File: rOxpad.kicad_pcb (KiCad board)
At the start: 2 copper layers, 77.8 x 63.5 mm, 22 parts, among them SW1 SW_Push, U1 ATmega32U4-A, Y1 16MHz

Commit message: might've forgot to save whoops
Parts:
- moved F1 83.7 mm to (107.2, 52.4), turned to 0 degrees
- moved C5 63.7 mm to (78.9, 106.6), turned to -90 degrees
- moved R4 61.6 mm to (93.5, 81.8), turned to 45 degrees
- moved C6 61.4 mm to (84.9, 100.0), turned to 45 degrees
- moved C2 60.5 mm to (82.6, 106.6), turned to -90 degrees
- moved U1 54.7 mm to (96.0, 92.1), turned to 45 degrees
- moved C1 53.1 mm to (86.4, 106.6), turned to -90 degrees
- moved MX1 50.1 mm to (76.8, 69.1)
- moved MX2 50.1 mm to (96.0, 69.1)
- moved MX3 50.1 mm to (115.1, 69.1)
- moved D1 49.0 mm to (85.1, 69.1)
- moved D2 49.0 mm to (104.1, 69.1)
- moved D3 49.0 mm to (123.2, 69.1)
- moved SW1 48.0 mm to (118.3, 92.9), turned to 180 degrees
- moved R1 46.2 mm to (106.4, 56.4), turned to 0 degrees
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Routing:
- net +5V: track 0.48 -> 79.0 mm, vias 0 -> 2
- net GND: track 0.61 -> 76.6 mm
- net ROW-0: track 0.00 -> 72.4 mm
- net Net-(R1-Pad2): track 0.00 -> 64.4 mm, vias 0 -> 2
- net Net-(R2-Pad2): track 0.00 -> 57.2 mm, vias 0 -> 2
- net COL-0: track 0.00 -> 49.1 mm
- net Net-(R3-Pad2): track 0.00 -> 37.1 mm
- net COL-2: track 0.00 -> 36.0 mm, vias 0 -> 2
- net COL-1: track 0.00 -> 32.5 mm, vias 0 -> 1
- net Net-(C6-Pad1): track 0.00 -> 15.6 mm, vias 0 -> 2
- net Net-(C3-Pad2): track 0.22 -> 12.9 mm
- net Net-(F1-Pad1): track 0.00 -> 9.07 mm
- net D+: track 2.60 -> 10.5 mm
- net Net-(R4-Pad2): track 0.00 -> 7.08 mm
- net Net-(D1-Pad2): track 0.00 -> 6.94 mm
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
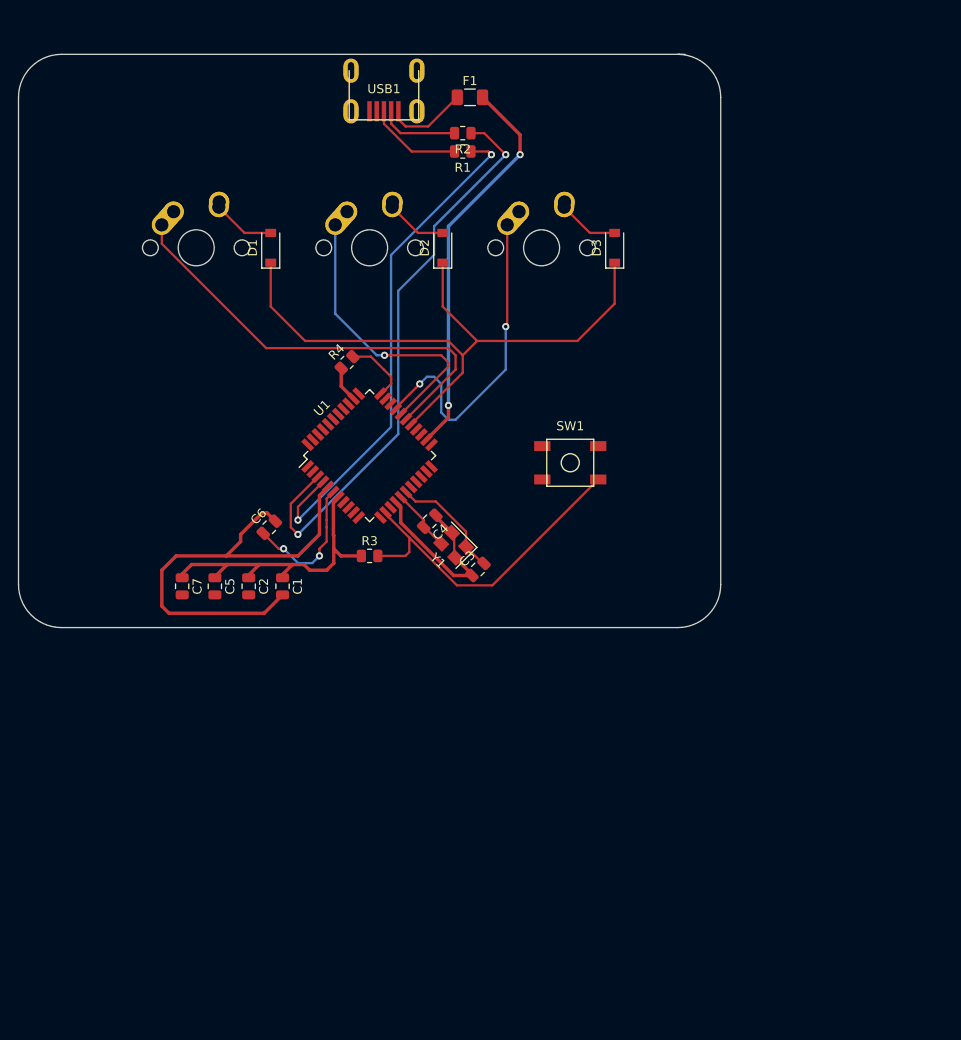
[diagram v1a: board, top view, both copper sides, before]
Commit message: started redesigning the schematic
didn't like the result lol
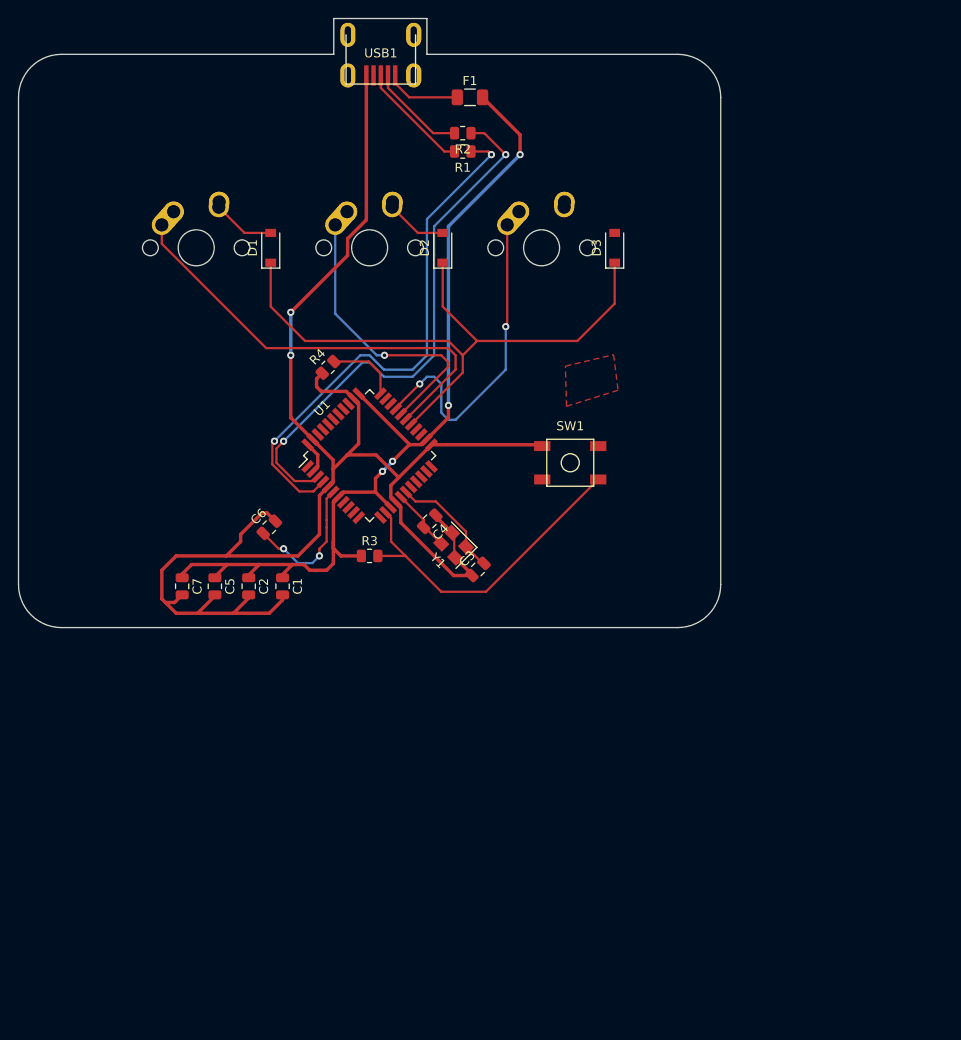
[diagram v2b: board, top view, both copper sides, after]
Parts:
- moved USB1 3.98 mm to (97.3, 45.5)
- moved R4 2.17 mm to (91.4, 82.3)
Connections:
- net Net-(C3-Pad2) renamed XTAL1
- net Net-(C4-Pad2) renamed XTAL2
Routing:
- net GND: track 76.6 -> 174.6 mm, vias 0 -> 2
- net +5V: track 79.0 -> 107.0 mm, vias 2 -> 4
- net Net-(D3-Pad2): track 6.78 -> 0.00 mm
- net Net-(R1-Pad2): track 64.4 -> 60.6 mm
- net Net-(R2-Pad2): track 57.2 -> 59.9 mm
- net D-: track 8.83 -> 10.8 mm
- net D+: track 10.5 -> 12.5 mm
- net Net-(R4-Pad2): track 7.08 -> 7.96 mm
- net Net-(F1-Pad1): track 9.07 -> 8.39 mm
- added copper zone on F.Cu, net GND
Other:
- board size 77.8 x 63.5 mm -> 77.8 x 67.5 mm

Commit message: I think it's finished wohoo
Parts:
- added R5: 5.1k, Resistor_SMD:R_0805_2012Metric_Pad1.20x1.40mm_HandSolder, F.Cu at (109.5, 72.2)
- added R6: 5.1k, Resistor_SMD:R_0805_2012Metric_Pad1.20x1.40mm_HandSolder, F.Cu at (100.0, 72.2)
- added U2: PRTR5V0U2X, random-keyboard-parts:SOT143B, F.Cu at (100.0, 76.2)
- C1: value 0.1uF -> 1uF; footprint Capacitor_SMD:C_0805_2012Metric -> Capacitor_SMD:C_0805_2012Metric_Pad1.18x1.45mm_HandSolder
- C2: value 0.1uF -> 22Pf; footprint Capacitor_SMD:C_0805_2012Metric -> Capacitor_SMD:C_0805_2012Metric_Pad1.18x1.45mm_HandSolder
- C3, C5: footprint Capacitor_SMD:C_0805_2012Metric -> Capacitor_SMD:C_0805_2012Metric_Pad1.18x1.45mm_HandSolder
- C4: value 22Pf -> 0.1uF; footprint Capacitor_SMD:C_0805_2012Metric -> Capacitor_SMD:C_0805_2012Metric_Pad1.18x1.45mm_HandSolder
- C6: value 1uF -> 0.1uF; footprint Capacitor_SMD:C_0805_2012Metric -> Capacitor_SMD:C_0805_2012Metric_Pad1.18x1.45mm_HandSolder
- C7: value 0.1uF -> 10uF; footprint Capacitor_SMD:C_0805_2012Metric -> Capacitor_SMD:C_0805_2012Metric_Pad1.18x1.45mm_HandSolder
- F1: value 500mA -> Polyfuse_Small; footprint Fuse:Fuse_1206_3216Metric -> Fuse:Fuse_1206_3216Metric_Pad1.42x1.75mm_HandSolder
- MX1, MX2, MX3: footprint MX_Alps_Hybrid:MX-1U-NoLED -> MX_Only:MXOnly-1U-Hotswap
- R1, R2, R3, R4: footprint Resistor_SMD:R_0805_2012Metric -> Resistor_SMD:R_0805_2012Metric_Pad1.20x1.40mm_HandSolder
- U1: value ATmega32U4-A -> ATmega16U2-A; footprint Package_QFP:TQFP-44_10x10mm_P0.8mm -> Package_QFP:TQFP-32_7x7mm_P0.8mm
- USB1: value Molex-0548190589 -> HRO-TYPE-C-31-M-12; footprint random-keyboard-parts:Molex-0548190589 -> Type-C:HRO-TYPE-C-31-M-12-HandSoldering
- moved C7 42.2 mm to (117.4, 108.3), turned to -135 degrees
- moved R4 38.1 mm to (97.6, 119.9), turned to 135 degrees
- moved C5 34.1 mm to (112.9, 103.8), turned to -135 degrees
- moved C1 33.2 mm to (119.1, 112.4), turned to -135 degrees
- moved C6 30.8 mm to (115.2, 106.0), turned to -135 degrees
- moved R3 27.8 mm to (119.1, 118.8), turned to 180 degrees
- moved U1 25.3 mm to (107.2, 114.8), turned to -45 degrees
- moved SW1 22.8 mm to (128.6, 113.2), turned to 0 degrees
- moved MX1 22.8 mm to (88.1, 88.9)
- moved MX2 22.7 mm to (107.2, 88.9)
- moved MX3 22.7 mm to (126.2, 88.9)
- moved C2 22.0 mm to (104.4, 103.3), turned to 135 degrees
- moved D1 21.6 mm to (95.2, 88.1)
- moved D2 21.6 mm to (114.3, 88.1)
- moved D3 21.6 mm to (133.3, 88.1)
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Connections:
- C1 pad 1: +5V -> Net-(C1-Pad1)
- C2 pad 1: +5V -> GND
- C2 pad 2: GND -> XTAL1
- C3 pad 2: XTAL1 -> XTAL2
- C4 pad 1: GND -> +5V
- C4 pad 2: XTAL2 -> GND
- C6 pad 1: Net-(C6-Pad1) -> +5V
- D1 pad 1: ROW-0 -> GND
- D2 pad 1: ROW-0 -> GND
- D3 pad 1: ROW-0 -> GND
- F1 pad 1: Net-(F1-Pad1) -> VCC
- MX1 pad 1: COL-0 -> KEY-0
- MX2 pad 1: COL-1 -> KEY-1
- MX3 pad 1: COL-2 -> KEY-2
- R4 pad 1: GND -> Net-(R4-Pad1)
- R4 pad 2: Net-(R4-Pad2) -> GND
- U1 pad 1: unconnected-(U1-Pad1) -> XTAL1
- U1 pad 13: Net-(R3-Pad2) -> Net-(R4-Pad1)
- U1 pad 14: +5V -> unconnected-(U1-Pad14)
- U1 pad 15: GND -> unconnected-(U1-Pad15)
- U1 pad 16: XTAL2 -> unconnected-(U1-Pad16)
- U1 pad 17: XTAL1 -> unconnected-(U1-Pad17)
- U1 pad 19: unconnected-(U1-Pad19) -> KEY-0
- U1 pad 2: +5V -> XTAL2
- U1 pad 20: unconnected-(U1-Pad20) -> KEY-1
- U1 pad 21: unconnected-(U1-Pad21) -> KEY-2
- U1 pad 23: GND -> unconnected-(U1-Pad23)
- U1 pad 24: +5V -> Net-(R3-Pad2)
- U1 pad 27: ROW-0 -> Net-(C1-Pad1)
- U1 pad 28: COL-0 -> GND
- U1 pad 29: COL-1 -> Net-(R2-Pad2)
- U1 pad 3: Net-(R1-Pad2) -> GND
- U1 pad 30: COL-2 -> Net-(R1-Pad2)
- U1 pad 31: unconnected-(U1-Pad31) -> +5V
- U1 pad 32: unconnected-(U1-Pad32) -> +5V
- U1 pad 4: Net-(R2-Pad2) -> +5V
- U1 pad 5: GND -> unconnected-(U1-Pad5)
- U1 pad 6: Net-(C6-Pad1) -> unconnected-(U1-Pad6)
- U1 pad 7: +5V -> unconnected-(U1-Pad7)
- USB1 pad 2: unconnected-(USB1-Pad2) -> VCC
- USB1 pad 3: D+ -> unconnected-(USB1-Pad3)
- USB1 pad 4: D- -> Net-(R5-Pad1)
- USB1 pad 5: Net-(F1-Pad1) -> D-
- USB1 pad 6: unconnected-(USB1-Pad6) -> D+
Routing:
- net ROW-0: track 72.4 -> 0.00 mm
- net KEY-2: track 0.00 -> 66.1 mm, vias 0 -> 1
- net KEY-0: track 0.00 -> 63.3 mm, vias 0 -> 1
- net COL-0: track 49.1 -> 0.00 mm
- net KEY-1: track 0.00 -> 48.0 mm, vias 0 -> 1
- net VCC: track 0.00 -> 42.7 mm, vias 0 -> 2
- net COL-2: track 36.0 -> 0.00 mm, vias 2 -> 0
- net COL-1: track 32.5 -> 0.00 mm, vias 1 -> 0
- net +5V: track 107.0 -> 80.6 mm, vias 4 -> 2
- net Net-(R3-Pad2): track 37.1 -> 19.8 mm
- net Net-(C6-Pad1): track 15.6 -> 0.00 mm, vias 2 -> 0
- net Net-(R2-Pad2): track 59.9 -> 75.5 mm
- net Net-(C1-Pad1): track 0.00 -> 14.0 mm
- net Net-(R1-Pad2): track 60.6 -> 72.5 mm
- net Net-(F1-Pad1): track 8.39 -> 0.00 mm
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- removed copper zone on F.Cu, net GND
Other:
- board size 77.8 x 67.5 mm -> 68.3 x 65.1 mm

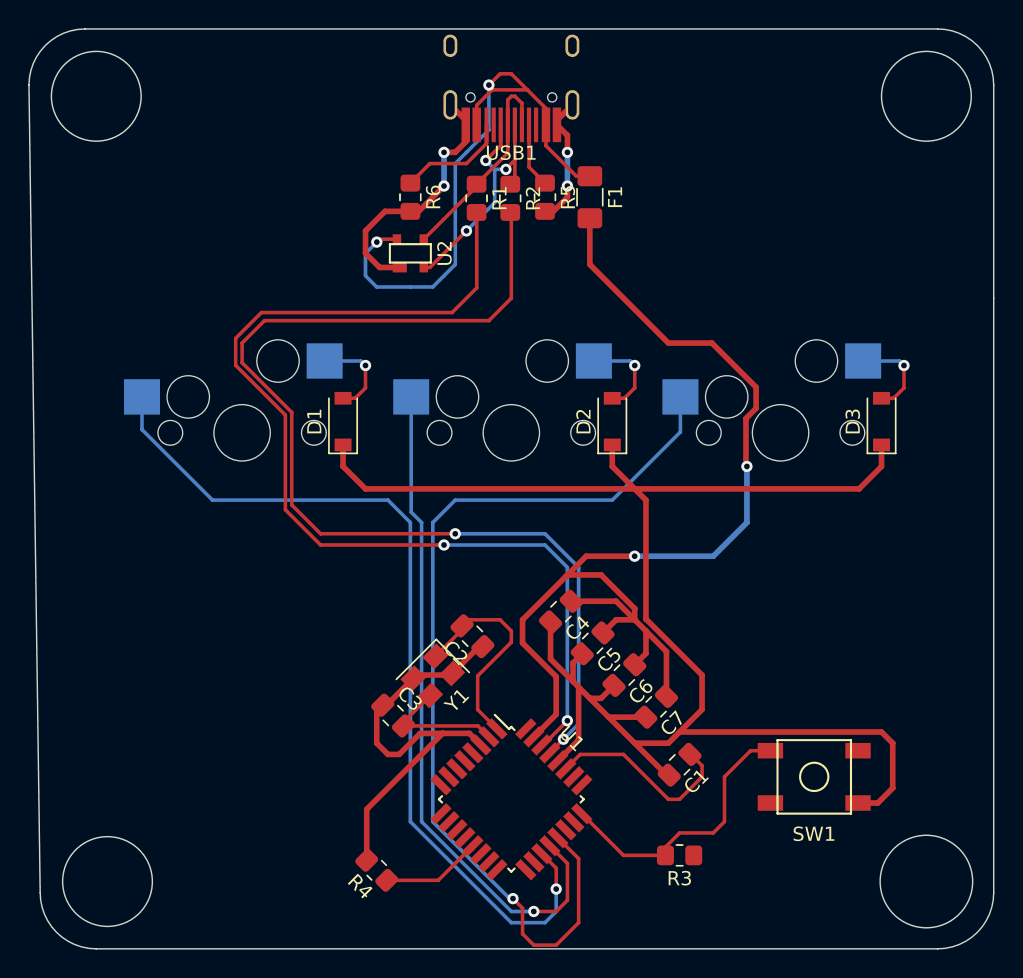
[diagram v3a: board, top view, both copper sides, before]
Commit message: create gitignore and change hole size
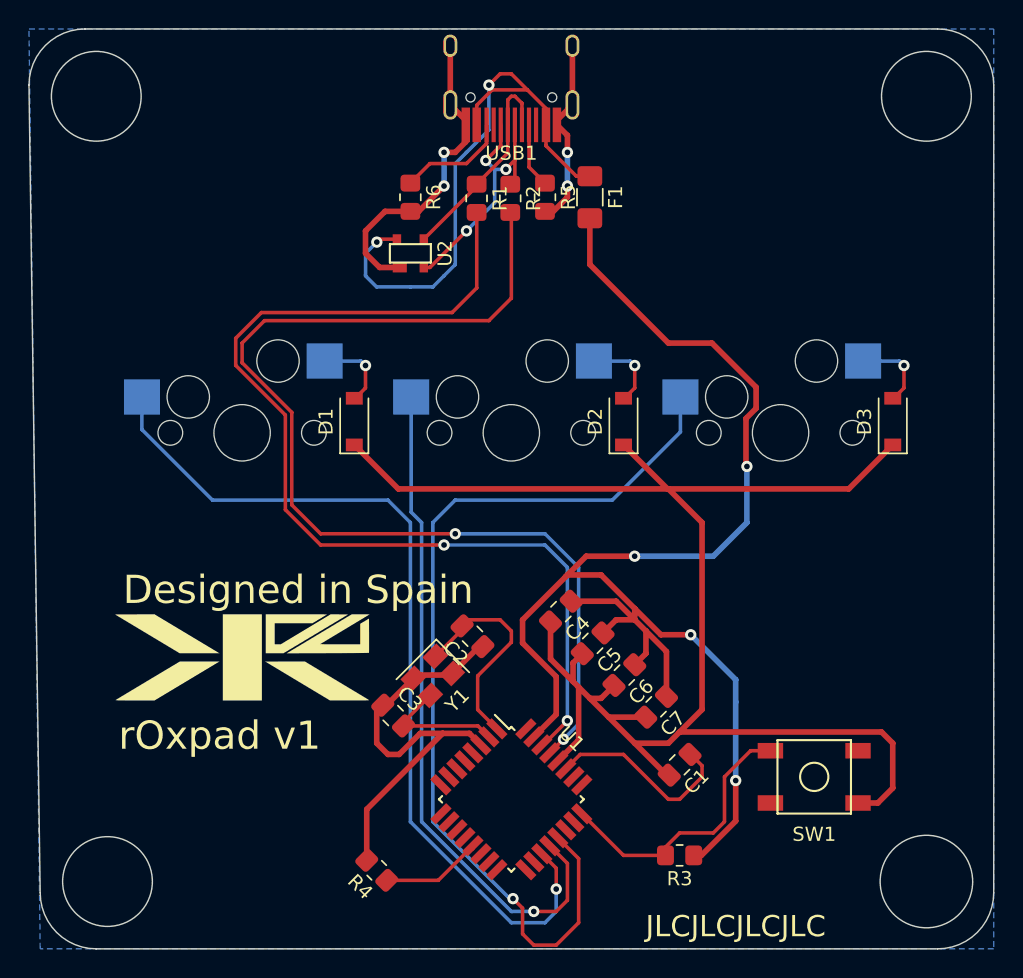
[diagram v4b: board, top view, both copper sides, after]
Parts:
- added G***: LOGO, LOGO, F.Cu at (88.1, 104.8)
- moved D3 0.79 mm to (134.1, 88.1)
- moved D1 0.79 mm to (96.0, 88.1)
- moved D2 0.79 mm to (115.1, 88.1)
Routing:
- net +5V: track 80.6 -> 103.8 mm, vias 2 -> 4
- net GND: track 177.7 -> 183.9 mm
- net Net-(D3-Pad2): track 6.50 -> 5.70 mm
- net Net-(D2-Pad2): track 6.50 -> 5.70 mm
- net Net-(D1-Pad2): track 6.50 -> 5.70 mm
- added copper zone on B.Cu, net GND
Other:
- board text added: "Designed in Spain"
- board text added: "JLCJLCJLCJLC"
- board text added: "rOxpad v1"

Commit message: Made some changes so it's doesn't explode
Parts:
- removed C6: 0.1uF, Capacitor_SMD:C_0805_2012Metric_Pad1.18x1.45mm_HandSolder
- moved C4 18.3 mm to (96.8, 113.5), turned to 90 degrees
- moved C7 7.37 mm to (114.3, 101.6), turned to -90 degrees
- moved C1 4.17 mm to (115.1, 111.1), turned to 90 degrees
- moved C5 4.01 mm to (115.1, 107.2), turned to -90 degrees
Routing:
- net GND: track 183.9 -> 145.0 mm
- net +5V: track 103.8 -> 83.6 mm
- net Net-(C1-Pad1): track 14.0 -> 4.50 mm
- net D-: track 15.2 -> 24.5 mm, vias 0 -> 2
- net KEY-1: track 48.0 -> 56.1 mm
- net VCC: track 42.7 -> 35.5 mm
- net KEY-0: track 63.3 -> 70.1 mm
- net KEY-2: track 66.1 -> 72.7 mm
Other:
- outline, holes or cut-outs redrawn
